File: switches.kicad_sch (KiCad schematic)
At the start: 29 parts, among them SW1 PEC164220F-S0024, SW2 ZX-QC66-7.5TP, SW3 291V1022F832AB, SW4 MS-22C01-G010, U2 MCP23S17_ML

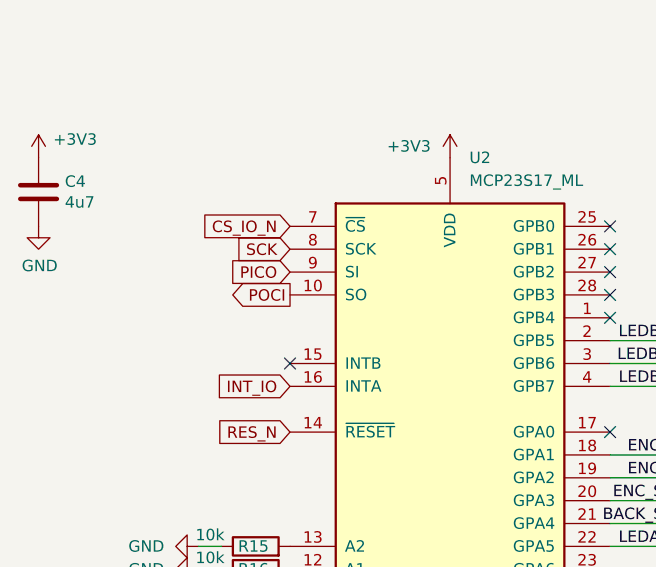
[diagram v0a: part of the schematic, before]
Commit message: rename POCI and PICO signals to SDO and SDI
according to the OSHWA recommendation
https://oshwa.org/resources/a-resolution-to-redefine-spi-signal-names/
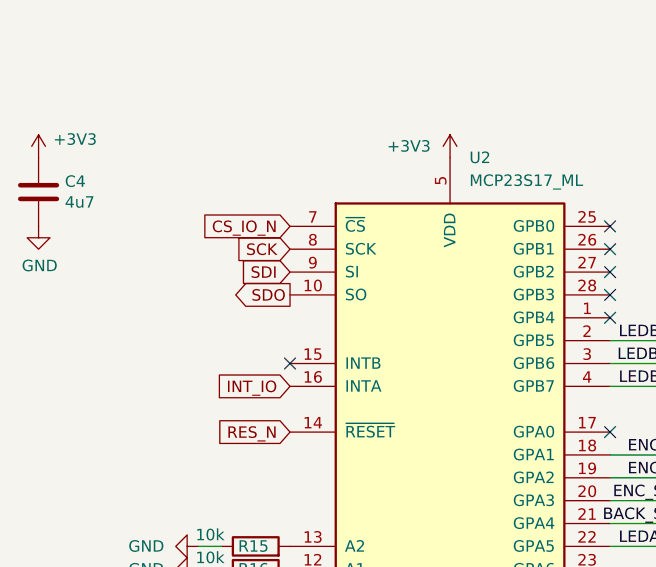
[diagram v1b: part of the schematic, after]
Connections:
- net PICO renamed SDI
- net POCI renamed SDO
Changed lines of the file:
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@@
 			"VQAAQLQVABi+GgAEAAAAnVUAAKA3gmudVQAAUEx8a51VAABAtBUAGL4aAAEAAACdVQAAUEx8a51V"
 			"AADQLY5rnVUAALB6FgAYvhoABAAAAJ1VAADgfndrnVUAAGAwgWudVQAAsHoWABi+GgABAAAAnVUA"
-			"AGAwgWudVQAAQA=="
+			"AGAwgWudVQAAQAIAAAAAAABAAAAAAAAAAA3caC88VgAACQAAAAAAAAAAAAAAAAAAAAAAAAAAAAAA"
+			"AAAAAAIAAAAAAAAAAAAAAAAAAAAAAAAAMQAAAAAAAACAMgRNOVYAAGDD+Ew5VgAAsN4HTTlWAAAB"
+			"AAAAAAAAABADAAAAAAAAUAAAAAAAAABtpHsvPFYAAHQvZm9udHMvdHJ1ZXR5cGUvbm90by9Ob3Rv"
+			"U2Fuc1RpZmluYWdoQVBULVJlZ3VsYXIudHRmAAAAAAAAAAAAAAChAwAAAAAAAGCEB005VgAAILcH"
+			"TTlWAAABAAAAAAAAAAEAAAAAAAAAAAAAAAAAAACBAgAAAAAAAODhB005VgAAgNcATTlWAAAgAAAA"
+			"AAAAACAAAAAAAAAAfTGTLjxWAACAAAAAAAAAAEAAAAAAAAAAMAAAAAAAAADtD5MuPFYAAAMAAAAA"
+			"AAAAoN8HTTlWAAABAAAAAAAAAHAAAAAAAAAAMAAAAAAAAADdBpQuPFYAAHMgVGlmaW5hZ2ggQWRy"
+			"YXIAAAAAAAAAAAAAAAAAAAAA4QEAAAAAAADg4QdNOVYAACAb/4pgfwAAAgAAAAAAAAAw4QdNOVYA"
+			"AAMAAAAAAAAA4OAHTTlWAAAVAAAAAAAAAPDhB005VgAAGAAAAAAAAABw4gdNOVYAACIAAAAAAAAA"
+			"gOEHTTlWAAAAAAAAAAAAAAAAAAAAAAAAAAAAAAAAAAAAAAAAAAAAAAAAAAAAAAAAAAAAAAAAAAAA"
+			"AAAAAAAAAAAAAAAAAAAAAAAAAAAAAAAAAAAAAAAAAAAAAAAAAAAAAAAAAAAAAAAAAAAAAAAAAAAA"
+			"AAAAAAAAAAAAAAAAAAAAAAAAAAAAAAAAAAAAAAAAAAAAAAAAAAAAAAAAAAAAAAAAAAAAAAAAEAEA"
+			"AAAAAAAwAAAAAAAAAF4xky48VgAAAwAAAAAAAAAQ4QdNOVYAAAEAAAAAAAAAAAAAAAAAAAAhAAAA"
+			"AAAAACDfB005VgAAYNQATTlWAABgAQAAAAAAADAAAAAAAAAAHg+TLjxWAAADAAAAAAAAAGDhB005"
+			"VgAAAQAAAAAAAAAAAAAAAAAAAFEAAAAAAAAAgGPvTDlWAABg4gdNOVYAACAAAAAAAAAAMAAAAAAA"
+			"AAAeMpMuPFYAAAgAAAAAAAAAsOEHTTlWAAABAAAAAAAAALACAAAAAAAAQAAAAAAAAACuBpQuPFYA"
+			"AAkAAAAAAAAAAAAAAAAAAAAAAAAAAAAAAAAAAAACAAAAAAAAAAAAAAAAAAAAAAAAADEAAAAAAAAA"
+			"YOIHTTlWAAAQ1wBNOVYAACDiB005VgAAAQAAAAAAAAAgAwAAAAAAAFAAAAAAAAAAPgGTLjxWAAB0"
+			"L2ZvbnRzL3RydQ=="
 		)
 	)
@@
 			"AAAAAAAAAAAAAAAAAAAAAAAAAAAAAAAAAAAAAAAAAAAAAAAAAAAAAAAAAAAAAAAAAAAAAAAAAAAA"
 			"AAAAAAAAAAAAAAAAAAAAAAAAAAAAAAAAAAAAAAAAAAAAAAAAAAAAAAAAAAAAAAAAAAAAAAAAAAAA"
+			"AAAAAAAAAAAAAAAAAAAAAAAAAAAAAAAAAAAAAAAAAAAAAAAAAAAAAAAAAAAAAAAAAAAAAAAAAAAA"
+			"AAAAAAAAAAAAAAAAAAAAAAAAAAAAAAAAAAAAAAAAAAAAAAAAAAAAAAAAAAAAAAAAAAAAAAAAAAAA"
+			"AAAAAAAAAAAAAAAAAAAAAAAAAAAAAAAAAAAAAAAAAAAAAAAAAAAAAAAAAAAAAAAAAAAAAAAAAAAA"
+			"AAAAAAAAAAAAAAAAAAAAAAAAAAAAAAAAAAAAAAAAAAAAAAAAAAAAAAAAAAAAAAAAAAAAAAAAAAAA"
+			"AAAAAAAAAAAAAAAAAAAAAAAAAAAAAAAAAAAAAAAAAAAAAAAAAAAAAAAAAAAAAAAAAAAAAAAAAAAA"
+			"AAAAAAAAAAAAAAAAAAAAAAAAAAAAAAAAAAAAAAAAAAAAAAAAAAAAAAAAAAAAAAAAAAAAAAAAAAAA"
+			"AAAAAAAAAAAAAAAAAAAAAAAAAAAAAAAAAAAAAAAAAAAAAAAAAAAAAAAAAAAAAAAAAAAAAAAAAAAA"
+			"AAAAAAAAAAAAAAAAAAAAAAAAAAAAAAAAAAAAAAAAAAAAAAAAAAAAAAAAAAAAAAAAAAAAAAAAAAAA"
+			"AAAAAAAAAAAAAAAAAAAAAAAAAAAAAAAAAAAAAAAAAAAAAAAAAAAAAAAAAAAAAAAAAAAAAAAAAAAA"
+			"AAAAAAAAAAAAAAAAAAAAAAAAAAAAAAAAAAAAAAAAAAAAAAAAAAAAAAAAAAAAAAAAAAAAAAAAAAAA"
+			"AAAAAAAAAAAAAAAAAAAAAAAAAAAAAAAAAAAAAAAAAAAAAAAAAAAAAAAAAAAAAAAAAAAAAAAAAAAA"
+			"AAAAAAAAAAAAAAAAAAAAAAAAAAAAAAAAAAAAAAAAAAAAAAAAAAAAAAAAAAAAAAAAAAAAAAAAAAAA"
+			"AAAAAAAAAAAAAAAAAAAAAAAAAAAAAAAAAAAAAAAAAAAAAAAAAAAAAAAAAAAAAAAAAAAAAAAAAAAA"
+			"AAAAAAAAAAAAAAAAAAAAAAAAAAAAAAAAAAAAAAAAAAAAAAAAAAAAAAAAAAAAAAAAAAAAAAAAAAAA"
+			"AAAAAAAAAAAAAAAAAAAAAAAAAAAAAAAAAAAAAAAAAAAAAAAAAAAAAAAAAAAAAAAAAAAAAAAAAAAA"
+			"AAAAAAAAAAAAAAAAAAAAAAAAAAAAAAAAAAAAAAAAAAAAAAAAAAAAAAAAAAAAAAAAAAAAAAAAAAAA"
+			"AAAAAAAAAAAAAAAAAAAAAAAAAAAAAAAAAAAAAAAAAAAAAAAAAAAAAAAAAAAAAAAAAAAAAAAAAAAA"
+			"AAAAAAAAAAAAAAAAAAAAAAAAAAAAAAAAAAAAAAAAAAAAAAAAAAAAAAAAAAAAAAAAAAAAAAAAAAAA"
 			"AAAAAA=="
 		)
@@
 			"AAAAAAAAAAAAAAAAAAAAAAAAAAAAAAAAAAAAAAAAAAAAAAAAAAAAAAAAAAAAAAAAAAAAAAAAAAAA"
 			"AAAAAAAAAAAAAAAAAAAAAAAAAAAAAAAAAAAAAAAAAAAAAAAAAAAAAAAAAAAAAAAAAAAAAAAAAAAA"
+			"AAAAAAAAAAAAAAAAAAAAAAAAAAAAAAAAAAAAAAAAAAAAAAAAAAAAAAAAAAAAAAAAAAAAAAAAAAAA"
+			"AAAAAAAAAAAAAAAAAAAAAAAAAAAAAAAAAAAAAAAAAAAAAAAAAAAAAAAAAAAAAAAAAAAAAAAAAAAA"
+			"AAAAAAAAAAAAAAAAAAAAAAAAAAAAAAAAAAAAAAAAAAAAAAAAAAAAAAAAAAAAAAAAAAAAAAAAAAAA"
+			"AAAAAAAAAAAAAAAAAAAAAAAAAAAAAAAAAAAAAAAAAAAAAAAAAAAAAAAAAAAAAAAAAAAAAAAAAAAA"
+			"AAAAAAAAAAAAAAAAAAAAAAAAAAAAAAAAAAAAAAAAAAAAAAAAAAAAAAAAAAAAAAAAAAAAAAAAAAAA"
+			"AAAAAAAAAAAAAAAAAAAAAAAAAAAAAAAAAAAAAAAAAAAAAAAAAAAAAAAAAAAAAAAAAAAAAAAAAAAA"
+			"AAAAAAAAAAAAAAAAAAAAAAAAAAAAAAAAAAAAAAAAAAAAAAAAAAAAAAAAAAAAAAAAAAAAAAAAAAAA"
+			"AAAAAAAAAAAAAAAAAAAAAAAAAAAAAAAAAAAAAAAAAAAAAAAAAAAAAAAAAAAAAAAAAAAAAAAAAAAA"
+			"AAAAAAAAAAAAAAAAAAAAAAAAAAAAAAAAAAAAAAAAAAAAAAAAAAAAAAAAAAAAAAAAAAAAAAAAAAAA"
+			"AAAAAAAAAAAAAAAAAAAAAAAAAAAAAAAAAAAAAAAAAAAAAAAAAAAAAAAAAAAAAAAAAAAAAAAAAAAA"
+			"AAAAAAAAAAAAAAAAAAAAAAAAAAAAAAAAAAAAAAAAAAAAAAAAAAAAAAAAAAAAAAAAAAAAAAAAAAAA"
+			"AAAAAAAAAAAAAAAAAAAAAAAAAAAAAAAAAAAAAAAAAAAAAAAAAAAAAAAAAAAAAAAAAAAAAAAAAAAA"
+			"AAAAAAAAAAAAAAAAAAAAAAAAAAAAAAAAAAAAAAAAAAAAAAAAAAAAAAAAAAAAAAAAAAAAAAAAAAAA"
+			"AAAAAAAAAAAAAAAAAAAAAAAAAAAAAAAAAAAAAAAAAAAAAAAAAAAAAAAAAAAAAAAAAAAAAAAAAAAA"
+			"AAAAAAAAAAAAAAAAAAAAAAAAAAAAAAAAAAAAAAAAAAAAAAAAAAAAAAAAAAAAAAAAAAAAAAAAAAAA"
+			"AAAAAAAAAAAAAAAAAAAAAAAAAAAAAAAAAAAAAAAAAAAAAAAAAAAAAAAAAAAAAAAAAAAAAAAAAAAA"
+			"AAAAAAAAAAAAAAAAAAAAAAAAAAAAAAAAAAAAAAAAAAAAAAAAAAAAAAAAAAAAAAAAAAAAAAAAAAAA"
+			"AAAAAAAAAAAAAAAAAAAAAAAAAAAAAAAAAAAAAAAAAAAAAAAAAAAAAAAAAAAAAAAAAAAAAAAAAAAA"
 			"AAAAAAAAAAAAAAAAAAAAAAAAAAAAAAAAAAAAAAAAAAAAAAAAAAAAAAAAAA=="
 		)
@@
 		)
 	)
-	(global_label "POCI"
+	(global_label "SDO"
 		(shape output)
 		(at 59.69 62.23 180)
@@
 		)
 		(property "Intersheetrefs" "${INTERSHEET_REFS}"
-			(at 52.8837 62.23 0)
+			(at 53.549 62.23 0)
 			(effects
 				(font
@@
 		)
 	)
-	(global_label "PICO"
+	(global_label "SDI"
 		(shape input)
 		(at 59.69 59.69 180)
@@
 		)
 		(property "Intersheetrefs" "${INTERSHEET_REFS}"
-			(at 52.8837 59.69 0)
+			(at 54.2747 59.69 0)
 			(effects
 				(font

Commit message: geographical re-annotate
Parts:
- renumbered C4 to C10, C5 to C11, C6 to C12, C7 to C13, C13 to C14, D2 to D1, D3 to D2, R17 to R11, R9 to R12, R8 to R13, R5 to R14, R11 to R17, R10 to R18, R6 to R19, R4 to R20, R3 to R21, R2 to R22, R1 to R23, R13 to R26, R12 to R27, R14 to R28, R26 to R29, SW2 to SW1, SW3 to SW2, SW1 to SW3, U2 to U4
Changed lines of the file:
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@@
 		(on_board yes)
 		(dnp no)
-		(property "Reference" "R3"
+		(property "Reference" "R21"
 			(at 218.44 33.02 90)
 			(effects
@@
 			(project "ui_board_1u"
 				(path "/3def8ca7-c7ff-40fd-acc8-d6d3f6c3eb5b/0f4f8b0f-462b-48e8-8b9f-43c0c112045e"
-					(reference "R3")
+					(reference "R21")
 					(unit 1)
 				)
@@
 		(on_board yes)
 		(dnp no)
-		(property "Reference" "R2"
+		(property "Reference" "R22"
 			(at 213.36 33.02 90)
 			(effects
@@
 			(project "ui_board_1u"
 				(path "/3def8ca7-c7ff-40fd-acc8-d6d3f6c3eb5b/0f4f8b0f-462b-48e8-8b9f-43c0c112045e"
-					(reference "R2")
+					(reference "R22")
 					(unit 1)
 				)
@@
 		(on_board yes)
 		(dnp no)
-		(property "Reference" "R1"
+		(property "Reference" "R23"
 			(at 208.28 33.02 90)
 			(effects
@@
 			(project "ui_board_1u"
 				(path "/3def8ca7-c7ff-40fd-acc8-d6d3f6c3eb5b/0f4f8b0f-462b-48e8-8b9f-43c0c112045e"
-					(reference "R1")
+					(reference "R23")
 					(unit 1)
 				)
@@
 		(on_board yes)
 		(dnp no)
-		(property "Reference" "C4"
+		(property "Reference" "C10"
 			(at 34.671 49.6316 0)
 			(effects
@@
 			(project "ui_board_1u"
 				(path "/3def8ca7-c7ff-40fd-acc8-d6d3f6c3eb5b/0f4f8b0f-462b-48e8-8b9f-43c0c112045e"
-					(reference "C4")
+					(reference "C10")
 					(unit 1)
 				)
@@
 		(on_board yes)
 		(dnp no)
-		(property "Reference" "R9"
+		(property "Reference" "R12"
 			(at 124.46 171.45 90)
 			(effects
@@
 			(project "ui_board_1u"
 				(path "/3def8ca7-c7ff-40fd-acc8-d6d3f6c3eb5b/0f4f8b0f-462b-48e8-8b9f-43c0c112045e"
-					(reference "R9")
+					(reference "R12")
 					(unit 1)
 				)
@@
 		(on_board yes)
 		(dnp no)
-		(property "Reference" "C7"
+		(property "Reference" "C13"
 			(at 174.498 70.104 0)
 			(effects
@@
 			(project "ui_board_1u"
 				(path "/3def8ca7-c7ff-40fd-acc8-d6d3f6c3eb5b/0f4f8b0f-462b-48e8-8b9f-43c0c112045e"
-					(reference "C7")
+					(reference "C13")
 					(unit 1)
 				)
@@
 		(on_board yes)
 		(dnp no)
-		(property "Reference" "R12"
+		(property "Reference" "R27"
 			(at 198.12 39.37 90)
 			(effects
@@
 			(project "ui_board_1u"
 				(path "/3def8ca7-c7ff-40fd-acc8-d6d3f6c3eb5b/0f4f8b0f-462b-48e8-8b9f-43c0c112045e"
-					(reference "R12")
+					(reference "R27")
 					(unit 1)
 				)
@@
 		(on_board yes)
 		(dnp no)
-		(property "Reference" "R13"
+		(property "Reference" "R26"
 			(at 198.12 44.45 90)
 			(effects
@@
 			(project "ui_board_1u"
 				(path "/3def8ca7-c7ff-40fd-acc8-d6d3f6c3eb5b/0f4f8b0f-462b-48e8-8b9f-43c0c112045e"
-					(reference "R13")
+					(reference "R26")
 					(unit 1)
 				)
@@
 		(on_board yes)
 		(dnp no)
-		(property "Reference" "R11"
+		(property "Reference" "R17"
 			(at 152.4 171.45 90)
 			(effects
@@
 			(project "ui_board_1u"
 				(path "/3def8ca7-c7ff-40fd-acc8-d6d3f6c3eb5b/0f4f8b0f-462b-48e8-8b9f-43c0c112045e"
-					(reference "R11")
+					(reference "R17")
 					(unit 1)
 				)
@@
 		(on_board yes)
 		(dnp no)
-		(property "Reference" "C5"
+		(property "Reference" "C11"
 			(at 164.338 70.104 0)
 			(effects
@@
 			(project "ui_board_1u"
 				(path "/3def8ca7-c7ff-40fd-acc8-d6d3f6c3eb5b/0f4f8b0f-462b-48e8-8b9f-43c0c112045e"
-					(reference "C5")
+					(reference "C11")
 					(unit 1)
 				)
@@
 		(on_board yes)
 		(dnp no)
-		(property "Reference" "R4"
+		(property "Reference" "R20"
 			(at 223.52 33.02 90)
 			(effects
@@
 			(project "ui_board_1u"
 				(path "/3def8ca7-c7ff-40fd-acc8-d6d3f6c3eb5b/0f4f8b0f-462b-48e8-8b9f-43c0c112045e"
-					(reference "R4")
+					(reference "R20")
 					(unit 1)
 				)
@@
 		(on_board yes)
 		(dnp no)
-		(property "Reference" "C13"
+		(property "Reference" "C14"
 			(at 182.626 70.104 0)
 			(effects
@@
 			(project "ui_board_1u"
 				(path "/3def8ca7-c7ff-40fd-acc8-d6d3f6c3eb5b/0f4f8b0f-462b-48e8-8b9f-43c0c112045e"
-					(reference "C13")
+					(reference "C14")
 					(unit 1)
 				)
@@
 		(dnp no)
 		(fields_autoplaced yes)
-		(property "Reference" "SW1"
+		(property "Reference" "SW3"
 			(at 259.08 34.29 0)
 			(effects
@@
 			(project "ui_board_1u"
 				(path "/3def8ca7-c7ff-40fd-acc8-d6d3f6c3eb5b/0f4f8b0f-462b-48e8-8b9f-43c0c112045e"
-					(reference "SW1")
+					(reference "SW3")
 					(unit 1)
 				)
@@
 		(on_board yes)
 		(dnp no)
-		(property "Reference" "C6"
+		(property "Reference" "C12"
 			(at 169.418 70.104 0)
 			(effects
@@
 			(project "ui_board_1u"
 				(path "/3def8ca7-c7ff-40fd-acc8-d6d3f6c3eb5b/0f4f8b0f-462b-48e8-8b9f-43c0c112045e"
-					(reference "C6")
+					(reference "C12")
 					(unit 1)
 				)
@@
 		(on_board yes)
 		(dnp no)
-		(property "Reference" "R17"
+		(property "Reference" "R11"
 			(at 55.626 95.25 90)
 			(effects
@@
 			(project "ui_board_1u"
 				(path "/3def8ca7-c7ff-40fd-acc8-d6d3f6c3eb5b/0f4f8b0f-462b-48e8-8b9f-43c0c112045e"
-					(reference "R17")
+					(reference "R11")
 					(unit 1)
 				)
@@
 		(on_board yes)
 		(dnp no)
-		(property "Reference" "R10"
+		(property "Reference" "R18"
 			(at 147.32 171.45 90)
 			(effects
@@
 			(project "ui_board_1u"
 				(path "/3def8ca7-c7ff-40fd-acc8-d6d3f6c3eb5b/0f4f8b0f-462b-48e8-8b9f-43c0c112045e"
-					(reference "R10")
+					(reference "R18")
 					(unit 1)
 				)
@@
 		(on_board yes)
 		(dnp yes)
-		(property "Reference" "SW3"
+		(property "Reference" "SW2"
 			(at 246.126 113.03 0)
 			(effects
@@
 			(project ""
 				(path "/3def8ca7-c7ff-40fd-acc8-d6d3f6c3eb5b/0f4f8b0f-462b-48e8-8b9f-43c0c112045e"
-					(reference "SW3")
+					(reference "SW2")
 					(unit 1)
 				)
@@
 		(on_board yes)
 		(dnp no)
-		(property "Reference" "R8"
+		(property "Reference" "R13"
 			(at 119.38 171.45 90)
 			(effects
@@
 			(project "ui_board_1u"
 				(path "/3def8ca7-c7ff-40fd-acc8-d6d3f6c3eb5b/0f4f8b0f-462b-48e8-8b9f-43c0c112045e"
-					(reference "R8")
+					(reference "R13")
 					(unit 1)
 				)
@@
 		(on_board yes)
 		(dnp no)
-		(property "Reference" "R6"
+		(property "Reference" "R19"
 			(at 142.24 171.45 90)
 			(effects
@@
 			(project "ui_board_1u"
 				(path "/3def8ca7-c7ff-40fd-acc8-d6d3f6c3eb5b/0f4f8b0f-462b-48e8-8b9f-43c0c112045e"
-					(reference "R6")
+					(reference "R19")
 					(unit 1)
 				)
@@
 		(on_board yes)
 		(dnp no)
-		(property "Reference" "R5"
+		(property "Reference" "R14"
 			(at 114.3 171.45 90)
 			(effects
@@
 			(project "ui_board_1u"
 				(path "/3def8ca7-c7ff-40fd-acc8-d6d3f6c3eb5b/0f4f8b0f-462b-48e8-8b9f-43c0c112045e"
-					(reference "R5")
+					(reference "R14")
 					(unit 1)
 				)
@@
 		(on_board yes)
 		(dnp no)
-		(property "Reference" "R26"
+		(property "Reference" "R29"
 			(at 198.12 59.69 90)
 			(effects
@@
 			(project "ui_board_1u"
 				(path "/3def8ca7-c7ff-40fd-acc8-d6d3f6c3eb5b/0f4f8b0f-462b-48e8-8b9f-43c0c112045e"
-					(reference "R26")
+					(reference "R29")
 					(unit 1)
 				)
@@
 		(on_board yes)
 		(dnp no)
-		(property "Reference" "D3"
+		(property "Reference" "D2"
 			(at 142.494 148.336 90)
 			(effects
@@
 			(project "ui_board_1u"
 				(path "/3def8ca7-c7ff-40fd-acc8-d6d3f6c3eb5b/0f4f8b0f-462b-48e8-8b9f-43c0c112045e"
-					(reference "D3")
+					(reference "D2")
 					(unit 1)
 				)
@@
 		(dnp no)
 		(fields_autoplaced yes)
-		(property "Reference" "U2"
+		(property "Reference" "U4"
 			(at 79.6133 46.99 0)
 			(effects
@@
 			(project "ui_board_1u"
 				(path "/3def8ca7-c7ff-40fd-acc8-d6d3f6c3eb5b/0f4f8b0f-462b-48e8-8b9f-43c0c112045e"
-					(reference "U2")
+					(reference "U4")
 					(unit 1)
 				)
@@
 		(on_board yes)
 		(dnp no)
-		(property "Reference" "R14"
+		(property "Reference" "R28"
 			(at 198.12 53.34 90)
 			(effects
@@
 			(project "ui_board_1u"
 				(path "/3def8ca7-c7ff-40fd-acc8-d6d3f6c3eb5b/0f4f8b0f-462b-48e8-8b9f-43c0c112045e"
-					(reference "R14")
+					(reference "R28")
 					(unit 1)
 				)
@@
 		(on_board yes)
 		(dnp no)
-		(property "Reference" "D2"
+		(property "Reference" "D1"
 			(at 114.046 148.59 90)
 			(effects
@@
 			(project ""
 				(path "/3def8ca7-c7ff-40fd-acc8-d6d3f6c3eb5b/0f4f8b0f-462b-48e8-8b9f-43c0c112045e"
-					(reference "D2")
+					(reference "D1")
 					(unit 1)
 				)
@@
 		(on_board yes)
 		(dnp no)
-		(property "Reference" "SW2"
+		(property "Reference" "SW1"
 			(at 257.302 59.436 0)
 			(effects
@@
 			(project "ui_board_1u"
 				(path "/3def8ca7-c7ff-40fd-acc8-d6d3f6c3eb5b/0f4f8b0f-462b-48e8-8b9f-43c0c112045e"
-					(reference "SW2")
+					(reference "SW1")
 					(unit 1)
 				)

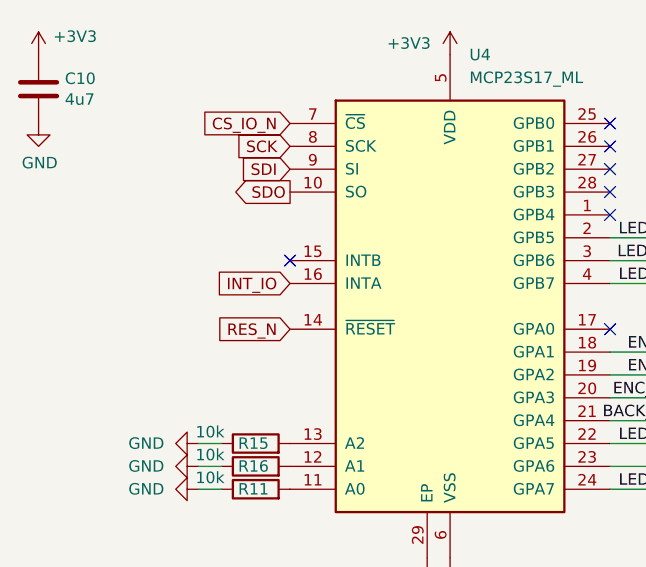
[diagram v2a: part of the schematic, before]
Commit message: review OLED pinout, add 2 GND pins
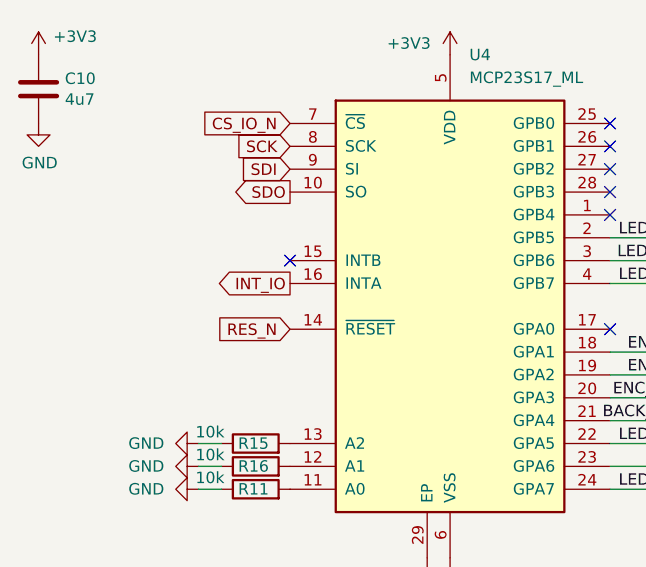
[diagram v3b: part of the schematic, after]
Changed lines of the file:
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@@
 	(title_block
 		(title "ui_board_1u - User interface board")
-		(date "2025-12-07")
+		(date "2025-12-17")
 		(rev "-")
 		(company "Betz Engineering")
@@
 	)
 	(global_label "INT_IO"
-		(shape input)
+		(shape output)
 		(at 59.69 72.39 180)
 		(fields_autoplaced yes)

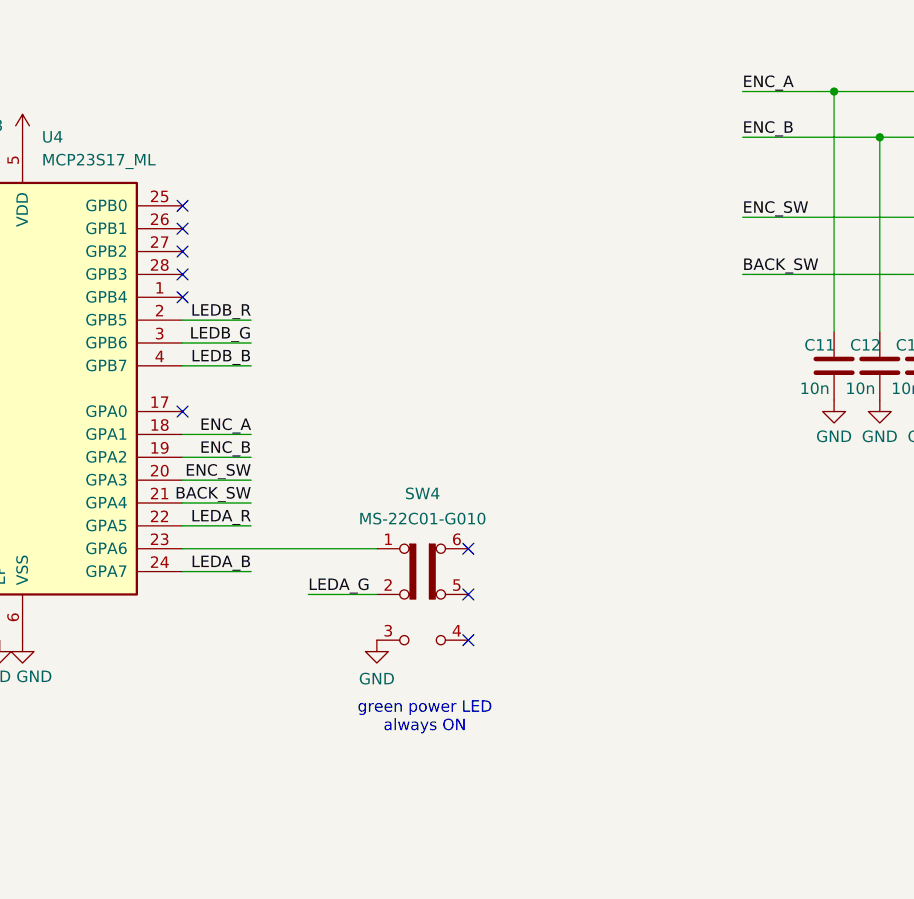
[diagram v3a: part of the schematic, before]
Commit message: add extension board connector
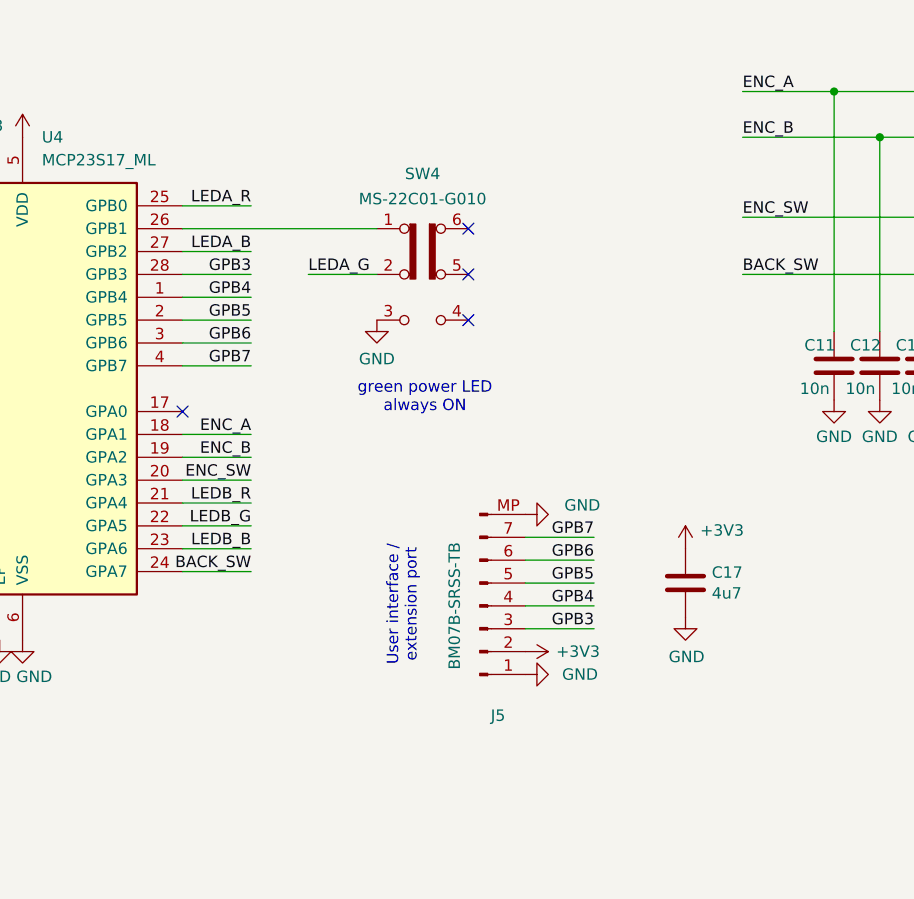
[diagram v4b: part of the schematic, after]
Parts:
- added C17: 4u7, Capacitor_SMD:C_1206_3216Metric, symbol Device:C
- added J5: BM07B-SRSS-TB, Connector_JST:JST_SH_BM07B-SRSS-TB_1x07-1MP_P1.00mm_Vertical, symbol Connector:Conn_01x07_Pin
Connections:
- net +3V3: now also C17.1, J5.2 (Pin_2)
- net BACK_SW: now also U4.24 (GPA7); no longer U4.21 (GPA4)
- net GND: now also C17.2, J5.1 (Pin_1), J5.MP
- net LEDA_B: now also U4.27 (GPB2); no longer U4.24 (GPA7)
- net LEDA_R: now also U4.25 (GPB0); no longer U4.22 (GPA5)
- net LEDB_B: now also U4.23 (GPA6); no longer U4.4 (GPB7)
- net LEDB_G: now also U4.22 (GPA5); no longer U4.3 (GPB6)
- net LEDB_R: now also U4.21 (GPA4); no longer U4.2 (GPB5)
- net GPB4: now reaches U4.1 (GPB4)
- net GPB4: now also J5.4 (Pin_4)
- net at SW4.1 (A): now also U4.26 (GPB1); no longer U4.23 (GPA6)
- net GPB3: now reaches U4.28 (GPB3)
- net GPB3: now also J5.3 (Pin_3)
- new net GPB5: J5.5 (Pin_5), U4.2 (GPB5)
- new net GPB6: J5.6 (Pin_6), U4.3 (GPB6)
- new net GPB7: J5.7 (Pin_7), U4.4 (GPB7)
- no-connect marks 10 -> 5
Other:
- note added: "User interface / extension port"
- moved on the sheet: SW4
